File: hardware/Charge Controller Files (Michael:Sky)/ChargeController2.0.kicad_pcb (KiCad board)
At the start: 2 copper layers, 90.2 x 95.9 mm, 90 parts, among them J1 GND_TEST_01x01_Pin, J10 SOL_TEST_01x01_Pin, J13 Conn-1x2, J14 Conn-1x2, J15 Conn-1x2, J17 SCL_MAS_01x01_Pin, J18 SDA_MAS_01x01_Pin, J19 SYS-1x2, J2 SP_01x02_Pin, J3 BATT_TEST_01x01_Pin, J4 3.3V_PULLUP_01x02_Pin, J5 BATT_01x02_Pin, J6 Conn-1x2, J7 Conn-1x2, J8 Conn-1x2, J9 SYS_TEST_01x01_Pin, Q1 SI2318DS-T1-E3, Q10 SI2318DS-T1-E3, Q11 SI2318DS-T1-E3, Q12 SI2318DS-T1-E3, Q2 SI2318DS-T1-E3, Q3 SI2318DS-T1-E3, Q4 SI2318DS-T1-E3, Q5 AONS66614, Q6 AONS66614, Q7 AONS66614, Q8 AONS66614, Q9 SI2318DS-T1-E3, SW1 100SP1T1B1M1QEH, U1 BQ25756ERRVR

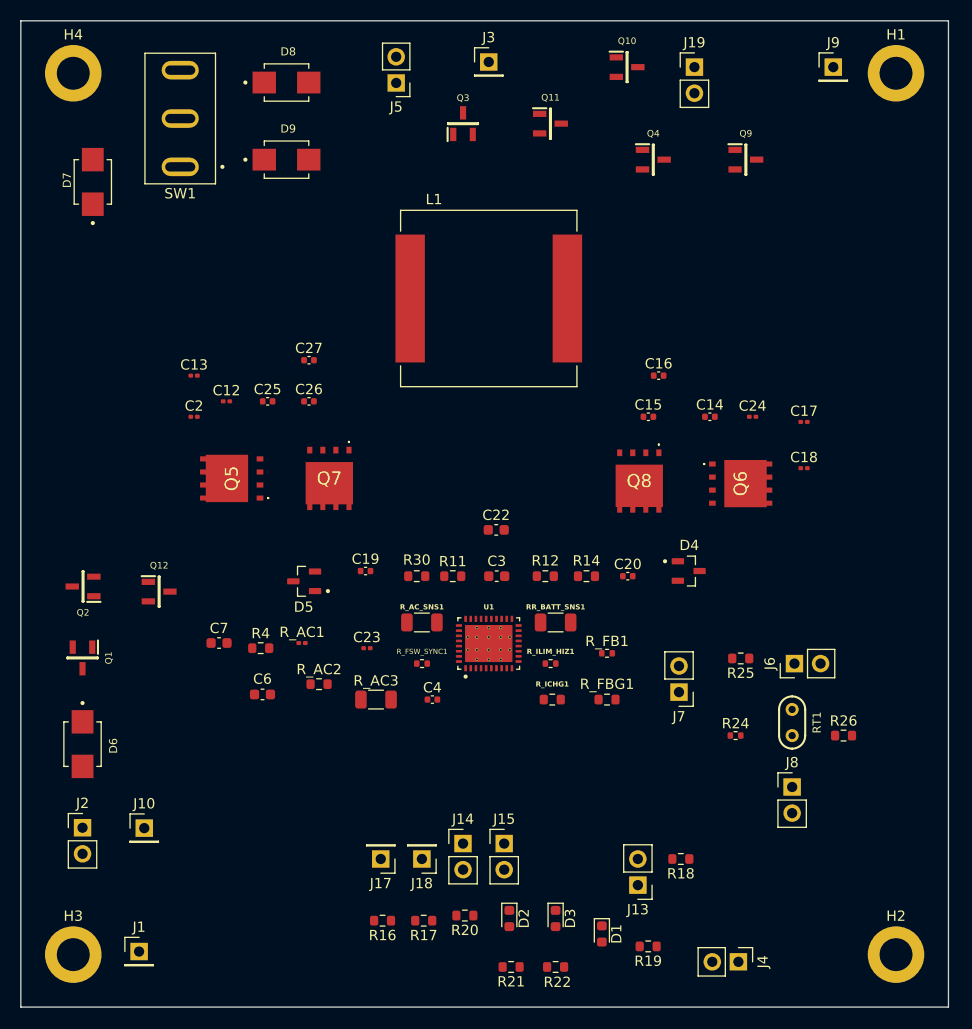
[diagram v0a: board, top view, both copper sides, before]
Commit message: PCB routing/MOSFET fix
- PCB routing
- MOSFET footprint fix (9 pins)
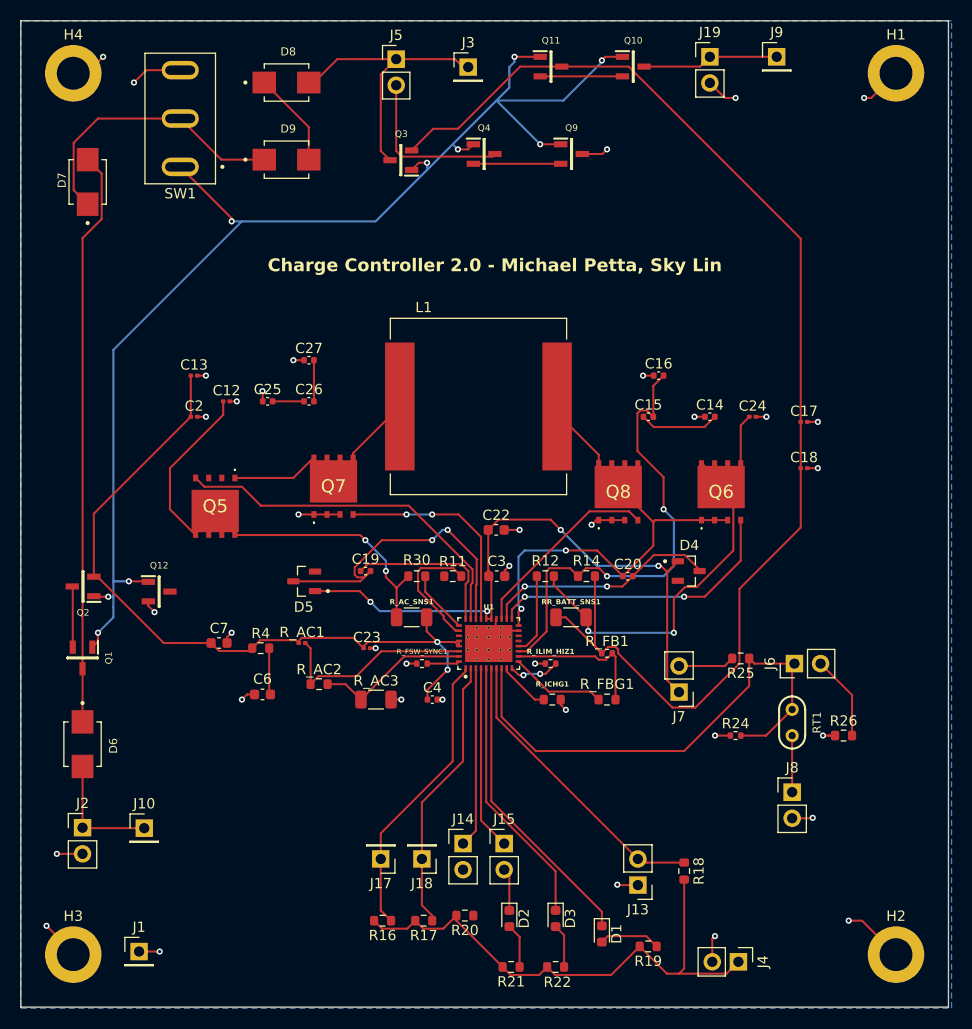
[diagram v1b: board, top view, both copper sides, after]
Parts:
- R_AC3: value 53.25k -> 53.25
- moved Q9 17.0 mm to (190.6, 49.5)
- moved Q4 16.5 mm to (182.1, 49.5)
- moved L1 10.5 mm to (181.5, 74.0)
- moved Q3 7.01 mm to (173.9, 50.0), turned to 180 degrees
- moved J9 5.59 mm to (210.5, 40.0)
- moved Q11 5.55 mm to (188.6, 41.0)
- moved Q5 3.14 mm to (155.9, 83.7), turned to 180 degrees
- moved J5 2.31 mm to (173.5, 40.2), turned to 0 degrees
- moved Q8 2.29 mm to (195.1, 82.3), turned to 0 degrees
- moved Q6 2.06 mm to (205.1, 82.3), turned to 0 degrees
- moved J3 2.06 mm to (180.5, 41.0)
- moved J19 1.80 mm to (204.0, 40.0)
- moved RR_BATT_SNS1 1.58 mm to (190.5, 94.5)
- moved R18 1.22 mm to (201.5, 119.2), turned to -90 degrees
- moved R_AC_SNS1 1.12 mm to (175.0, 94.5)
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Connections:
- Q5 pad 9: (no net) -> Net-(Q5-D_1)
- Q6 pad 9: (no net) -> Net-(Q6-D_1)
- Q7 pad 9: (no net) -> /SW1
- Q8 pad 9: (no net) -> /SW2
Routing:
- net /EN: track 0.00 -> 126.0 mm, vias 0 -> 9
- net Net-(Q11-DRAIN): track 0.00 -> 123.7 mm
- net VAC: track 0.00 -> 73.9 mm, vias 0 -> 2
- net GND: track 0.00 -> 72.1 mm, vias 0 -> 37
- net /DRV_SUP: track 0.00 -> 61.2 mm, vias 0 -> 4
- net Net-(Q1-DRAIN): track 0.00 -> 56.0 mm
- net Net-(J4-Pin_1): track 0.00 -> 52.3 mm
- net /TS: track 0.00 -> 50.7 mm
- net /SRN: track 0.00 -> 45.9 mm, vias 0 -> 2
- net /SW2: track 0.00 -> 44.1 mm, vias 0 -> 2
- net Net-(Q6-D_1): track 0.00 -> 40.8 mm, vias 0 -> 2
- net Net-(Q5-D_1): track 0.00 -> 39.4 mm, vias 0 -> 2
- net /HIDRV_1: track 0.00 -> 35.5 mm
- net /SW1: track 0.00 -> 31.2 mm
- net /BTST_1: track 0.00 -> 30.9 mm, vias 0 -> 2
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- added copper zone on B.Cu, net GND
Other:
- board text added: "Charge Controller 2.0 - Michael Petta, Sky Lin"

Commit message: PCB routing
More PCB routing
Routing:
- net PGND: track 4.36 -> 58.1 mm, vias 0 -> 2
- net /SRP: track 15.7 -> 60.6 mm, vias 0 -> 2
- net /ACP: track 15.3 -> 40.9 mm, vias 0 -> 2
- net /ACN: track 10.2 -> 35.1 mm, vias 0 -> 2

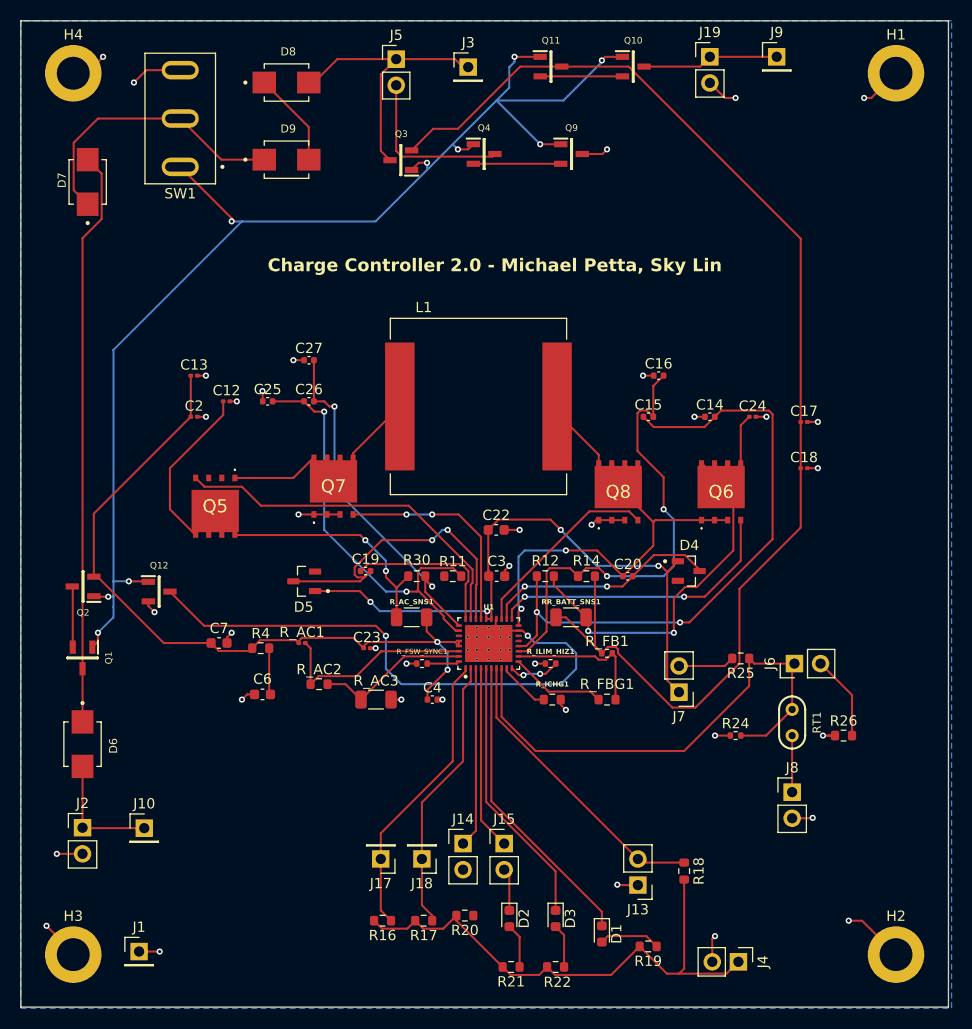
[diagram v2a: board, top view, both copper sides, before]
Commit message: PCB fixes
Routing fixes, removed redundent vias, fixed thermal spoke nets, changed min. annular width to 1.3.
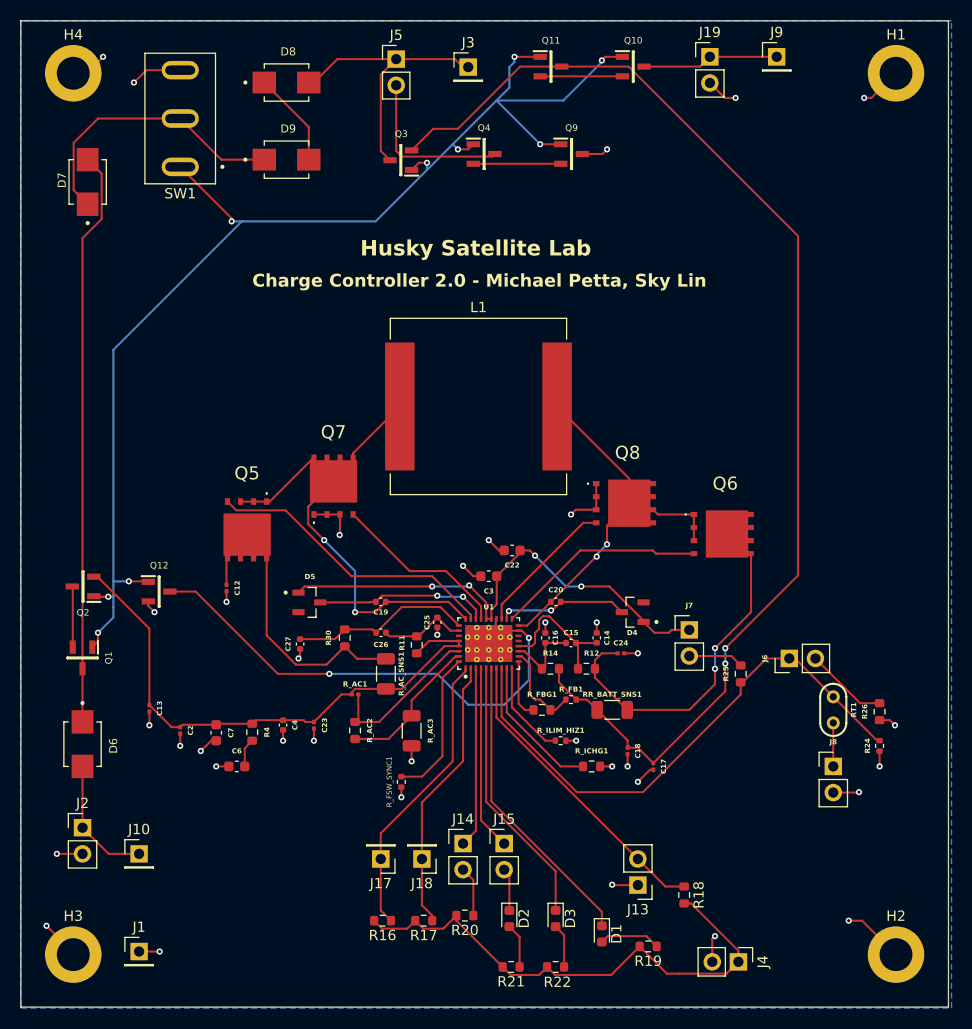
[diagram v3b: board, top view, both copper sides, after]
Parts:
- moved C17 36.6 mm to (198.5, 109.0), turned to -90 degrees
- moved C13 32.6 mm to (149.5, 103.3), turned to -90 degrees
- moved C18 32.4 mm to (196.0, 107.5), turned to -90 degrees
- moved C2 30.5 mm to (152.5, 105.5), turned to -90 degrees
- moved C16 27.8 mm to (188.0, 96.5), turned to -90 degrees
- moved C27 27.6 mm to (164.2, 97.1), turned to 90 degrees
- moved C25 27.1 mm to (177.5, 95.0), turned to 90 degrees
- moved C24 26.3 mm to (195.3, 98.0)
- moved C14 24.2 mm to (193.0, 96.5), turned to -90 degrees
- moved C26 23.6 mm to (172.0, 96.0), turned to 180 degrees
- moved C15 23.2 mm to (190.5, 97.0), turned to 180 degrees
- moved C12 18.2 mm to (157.0, 91.7), turned to -90 degrees
- moved C4 14.7 mm to (162.5, 105.0), turned to -90 degrees
- moved R24 14.0 mm to (220.5, 107.0), turned to 90 degrees
- moved R_FSW_SYNC1 11.7 mm to (174.0, 110.5), turned to 90 degrees
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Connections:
- U1 pad 38: (no net) -> PGND
- U1 pad 39: (no net) -> PGND
- U1 pad 40: (no net) -> PGND
- U1 pad 41: (no net) -> PGND
- U1 pad 42: (no net) -> PGND
- U1 pad 43: (no net) -> PGND
- U1 pad 44: (no net) -> PGND
- U1 pad 45: (no net) -> PGND
- U1 pad 46: (no net) -> PGND
- U1 pad 47: (no net) -> PGND
- U1 pad 48: (no net) -> PGND
- U1 pad 49: (no net) -> PGND
- U1 pad 50: (no net) -> PGND
- U1 pad 51: (no net) -> PGND
- U1 pad 52: (no net) -> PGND
- U1 pad 53: (no net) -> PGND
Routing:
- net /SRP: track 60.6 -> 13.6 mm, vias 2 -> 0
- net /SRN: track 45.9 -> 7.66 mm, vias 2 -> 0
- net /ACP: track 40.9 -> 8.53 mm, vias 2 -> 0
- net VAC: track 73.9 -> 55.1 mm, vias 2 -> 0
- net /ACN: track 35.1 -> 17.8 mm, vias 2 -> 0
- net Net-(Q5-D_1): track 39.4 -> 24.4 mm, vias 2 -> 0
- net /BTST_1: track 30.9 -> 16.9 mm
- net /DRV_SUP: track 61.2 -> 49.1 mm
- net /SW1: track 31.2 -> 43.2 mm, vias 0 -> 2
- net Net-(U1-FSW_SYNC): track 3.16 -> 14.7 mm
- net /BTST_2: track 22.9 -> 12.8 mm
- net GND: track 72.1 -> 81.1 mm
- net Net-(U1-ICHG): track 5.05 -> 13.9 mm
- net Net-(Q6-D_1): track 40.8 -> 32.3 mm
- net /HIDRV_2: track 29.1 -> 20.6 mm, vias 2 -> 0
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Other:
- board text added: "Husky Satellite Lab"
